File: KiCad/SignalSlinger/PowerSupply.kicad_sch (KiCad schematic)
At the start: 54 parts, among them J201 Barrel_Jack_Switch, J203 External Fan Power, J204 Controlled Power, Q201 RJK0354DSP, U201 LP2985-3.3, U202 LP2985-3.3, U203 TO-220 ADJ Reg., U204 TPS22810DBVT, U205 uA7805, U206 MIC2196YM

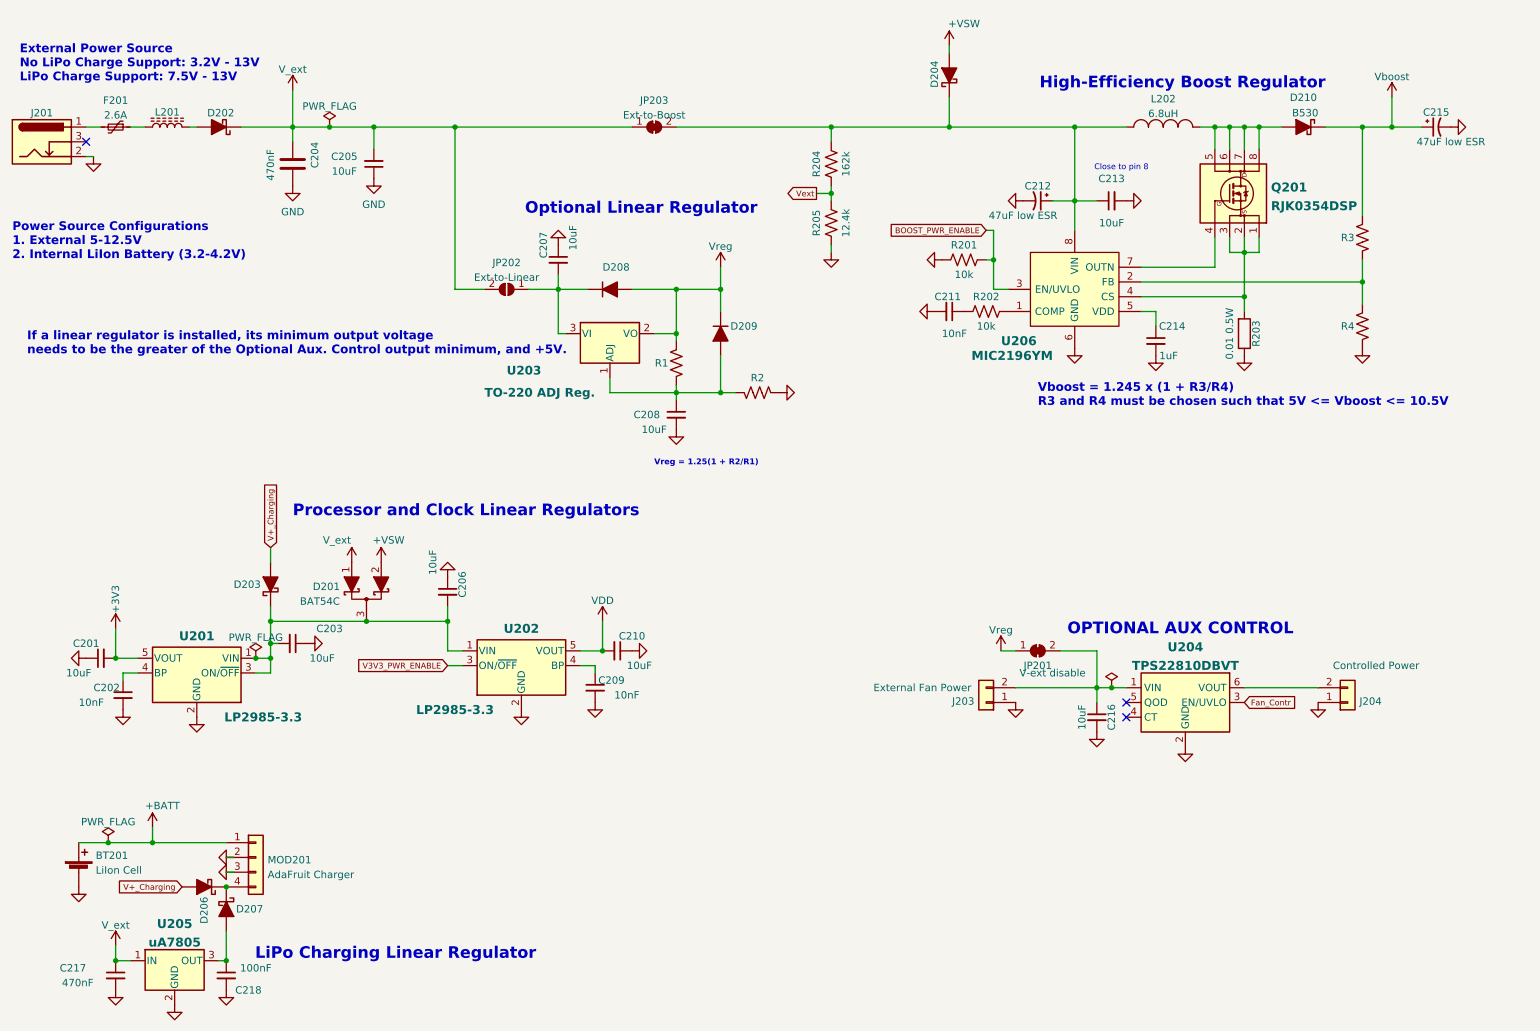
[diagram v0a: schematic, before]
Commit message: BOM Corrections
o Updated BOM
o Updated Footprints
o Updated PCB and Gerbers
o Updated schematic
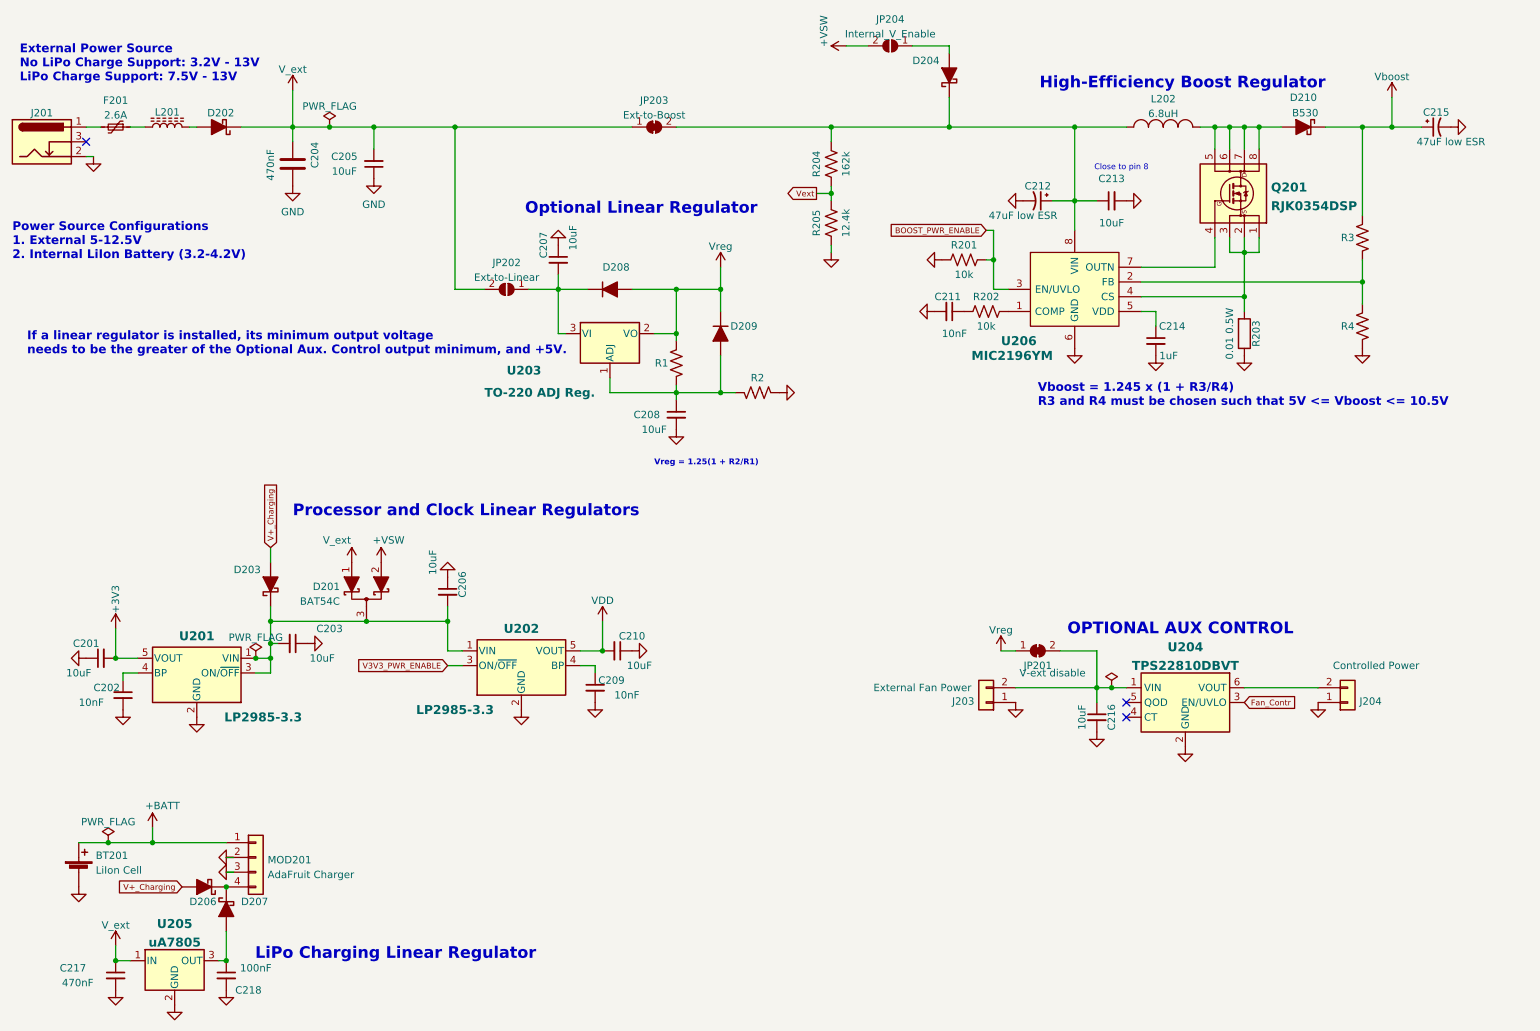
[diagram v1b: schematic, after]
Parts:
- added JP204: Internal_V_Enable, Jumper:SolderJumper-2_P1.3mm_Open_RoundedPad1.0x1.5mm, symbol Jumper:SolderJumper_2_Open
- D202: footprint Diode_SMD:D_SMB -> Diode_SMD:D_SMA
- D203, D204, D206, D207: Digi-Key Part No. RB070MM-30CT-ND -> CRS09QCT-ND; Link https://www.digikey.com/en/products/detail/rohm-semiconduct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 -> (none); Manufacturer Rohm Semiconductor -> Toshiba Semiconductor and Storage; Manufacturer PN RB070MM-30TR -> CRS09(TE85L,Q,M)
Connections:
- net +VSW: now also JP204.2 (B); no longer D204.2 (A)
- new net: D204.2 (A), JP204.1 (A)

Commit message: Design Updates
oThe boost regulator was removed from the design.
oAn additional load switch was added to the design.
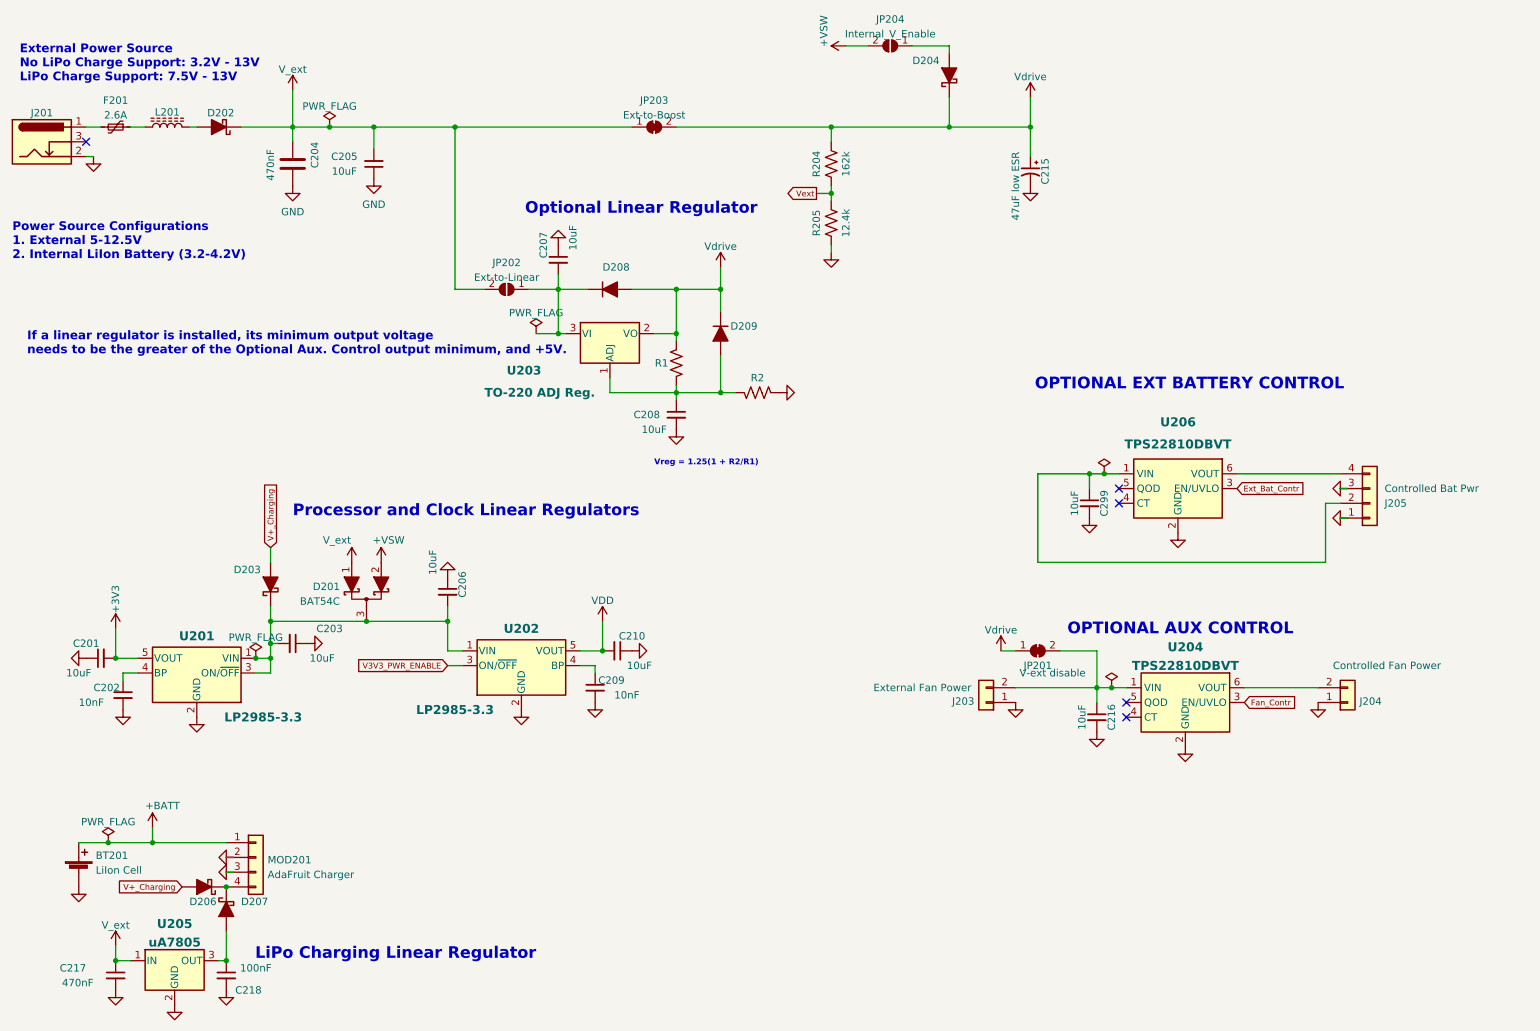
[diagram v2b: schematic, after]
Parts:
- removed C211: 10nF, Capacitor_SMD:C_0805_2012Metric, symbol Device:C_Small
- removed C212: 47uF low ESR, Capacitors:C_2917, symbol Device:CP1_Small-Device
- removed C213: 10uF, Capacitor_SMD:C_0805_2012Metric, symbol Device:C_Small
- removed C214: 1uF, Capacitor_SMD:C_0805_2012Metric, symbol Device:C_Small
- removed D210: B530, Diode_SMD:D_SMC, symbol Diode:D_Schottky_B530
- removed L202: 6.8uH, Inductors:CDR7D28MN, symbol Device:INDUCTOR_CDR7D28MN
- removed Q201: RJK0354DSP, Package_SO:SOIC-8_3.9x4.9mm_P1.27mm, symbol Transistor_FET:RJK0354DSP
- removed R201, R202: 10k, Resistor_SMD:R_0805_2012Metric, symbol Device:R_Small_US
- removed R203: 0.01 0.5W, Resistor_SMD:R_0805_2012Metric, symbol Device:R
- removed R3, R4: TBD, Resistor_THT:R_Axial_DIN0204_L3.6mm_D1.6mm_P2.54mm_Vertical, symbol Device:R_Small_US
- removed U206: MIC2196YM, Package_SO:SOIC-8_3.9x4.9mm_P1.27mm, symbol Regulator_Switching:MIC2196YM
- added C299: 10uF, Capacitor_SMD:C_0805_2012Metric, symbol Device:C_Small
- added J205: Controlled Bat Pwr, TerminalBlock:TerminalBlock_AdaFruitx2_1x02_P3.50mm_Horizontal, symbol Connector_Generic:Conn_01x04
- added U206: TPS22810DBVT, Package_TO_SOT_SMD:SOT-23-6, symbol Power_Management:TPS22810DBVT
- J204: value Controlled Power -> Controlled Fan Power
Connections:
- net GND: now also C299.2, J205.1 (Pin_1), J205.3 (Pin_3), U206.2 (GND)
- net Vdrive: now also D204.1 (K), JP203.2 (B), R204.2
- new net: C299.1, J205.2 (Pin_2), U206.1 (VIN)
- new net: J205.4 (Pin_4), U206.6 (VOUT)
- new net Ext_Bat_Contr: U206.3 (EN/UVLO)
- no-connect marks 3 -> 5
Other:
- note added: "OPTIONAL EXT BATTERY CONTROL"
- note removed: "Close to pin 8"
- note removed: "High-Efficiency Boost Regulator"
- note removed: "Vboost = 1.245 x (1 + R3/R4) R3 and R4 must be chosen such that 5V <= Vboost <= 10.5V"
- moved on the sheet: C215

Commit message: Production Updates
Corrects copper spacing issues
Removes warnings
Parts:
- BT201: symbol Device:Battery_Cell -> SignalSlinger Library:Battery_Cell
- C215: footprint Capacitors:C_2917 -> SignalSlinger_Footprints:C_2917; symbol Device:CP1_Small-Device -> SignalSlinger Library:CP1_Small-Device
- D201: symbol Device:D_Schottky_Dual_CommonCathode_AAK_Parallel -> SignalSlinger Library:D_Schottky_Dual_CommonCathode_AAK_Parallel
- D202: symbol Device:D_Schottky_Filled -> SignalSlinger Library:D_Schottky_Filled
- D203, D204, D206, D207: footprint Diode_SMD:D_SOD-123FL -> SignalSlinger_Footprints:D_SOD-123FL; symbol Device:D_Schottky_Filled -> SignalSlinger Library:D_Schottky_Filled
- D208, D209: symbol Diode:1N914WT -> SignalSlinger Library:1N914WT
- J201: symbol Connector:Barrel_Jack_Switch -> SignalSlinger Library:Barrel_Jack_Switch
- J205: footprint TerminalBlock:TerminalBlock_AdaFruitx2_1x02_P3.50mm_Horizontal -> SignalSlinger_Footprints:TerminalBlock_4Ucon_1x02_P3.50mm_Horizontal; symbol Connector_Generic:Conn_01x04 -> SignalSlinger Library:Conn_01x04
- JP201, JP203: symbol Jumper:SolderJumper_2_Bridged -> SignalSlinger Library:SolderJumper_2_Bridged
- JP202, JP204: symbol Jumper:SolderJumper_2_Open -> SignalSlinger Library:SolderJumper_2_Open
- L201: footprint Inductor_SMD:WPN4020H2R2MT -> SignalSlinger_Footprints:WPN4020H2R2MT
- MOD201: symbol Connector_Generic:Conn_01x04 -> SignalSlinger Library:Conn_01x04
- R1, R2, R204, R205: symbol Device:R_Small_US -> SignalSlinger Library:R_Small_US
- U204, U206: symbol Power_Management:TPS22810DBVT -> SignalSlinger Library:TPS22810DBVT
- U205: footprint Package_TO_SOT_SMD:SOT-223-4 -> SignalSlinger_Footprints:SOT-223-4
